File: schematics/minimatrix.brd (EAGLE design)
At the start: 32 x 32 mm, 10 parts

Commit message: ?
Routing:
- net N$2: track 70.4 -> 0.00 mm, vias 1 -> 0
- net GND: track 48.4 -> 0.00 mm, vias 1 -> 0
- net N$9: track 42.3 -> 0.00 mm, vias 3 -> 0
- net N$10: track 41.2 -> 0.00 mm, vias 1 -> 0
- net N$4: track 34.7 -> 0.00 mm
- net VCC: track 32.7 -> 0.00 mm, vias 1 -> 0
- net N$8: track 28.4 -> 0.00 mm
- net N$3: track 26.8 -> 0.00 mm
- net R6: track 25.4 -> 0.00 mm, vias 1 -> 0
- net R3: track 22.8 -> 0.00 mm
- net R8: track 22.2 -> 0.00 mm
- net C6: track 21.5 -> 0.00 mm, vias 1 -> 0
- net ROW1: track 20.3 -> 0.00 mm, vias 1 -> 0
- net R2: track 19.9 -> 0.00 mm, vias 1 -> 0
- net N$6: track 18.4 -> 0.00 mm, vias 1 -> 0
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
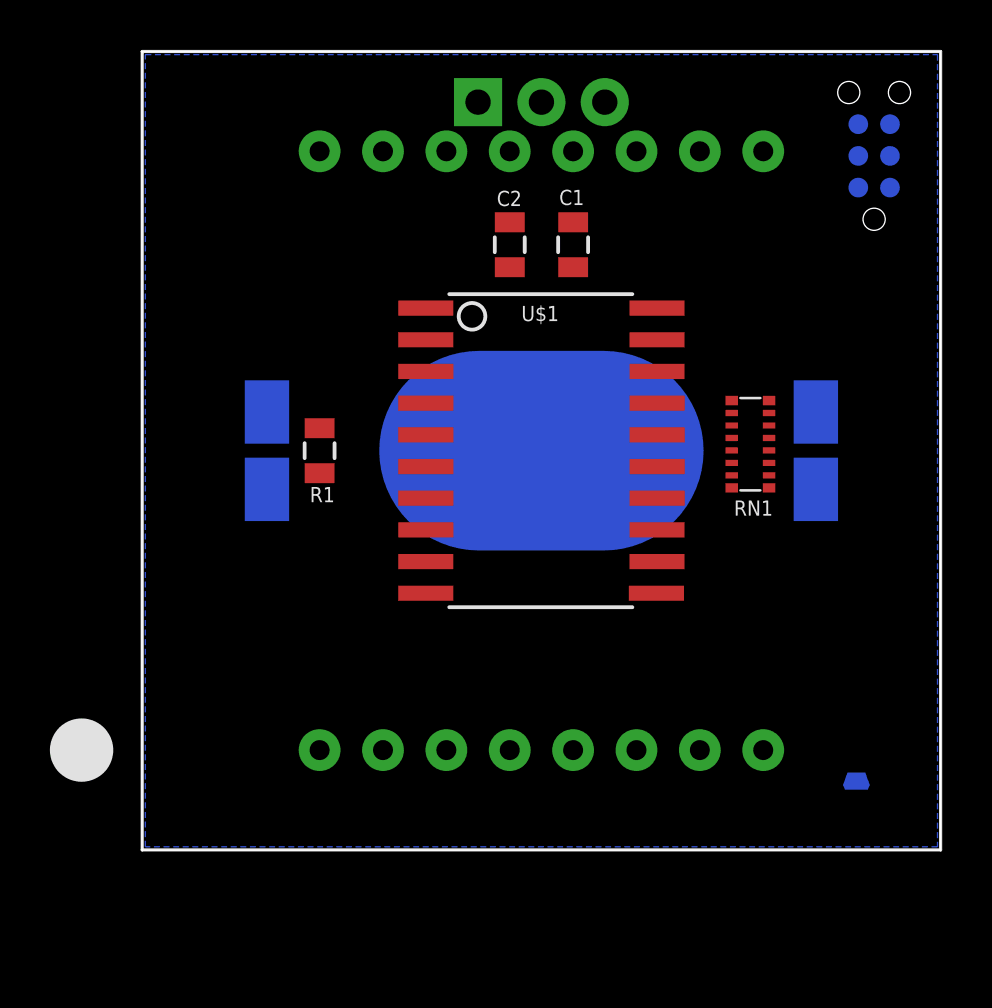
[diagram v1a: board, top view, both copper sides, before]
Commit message: Update design restoring IR receiver.
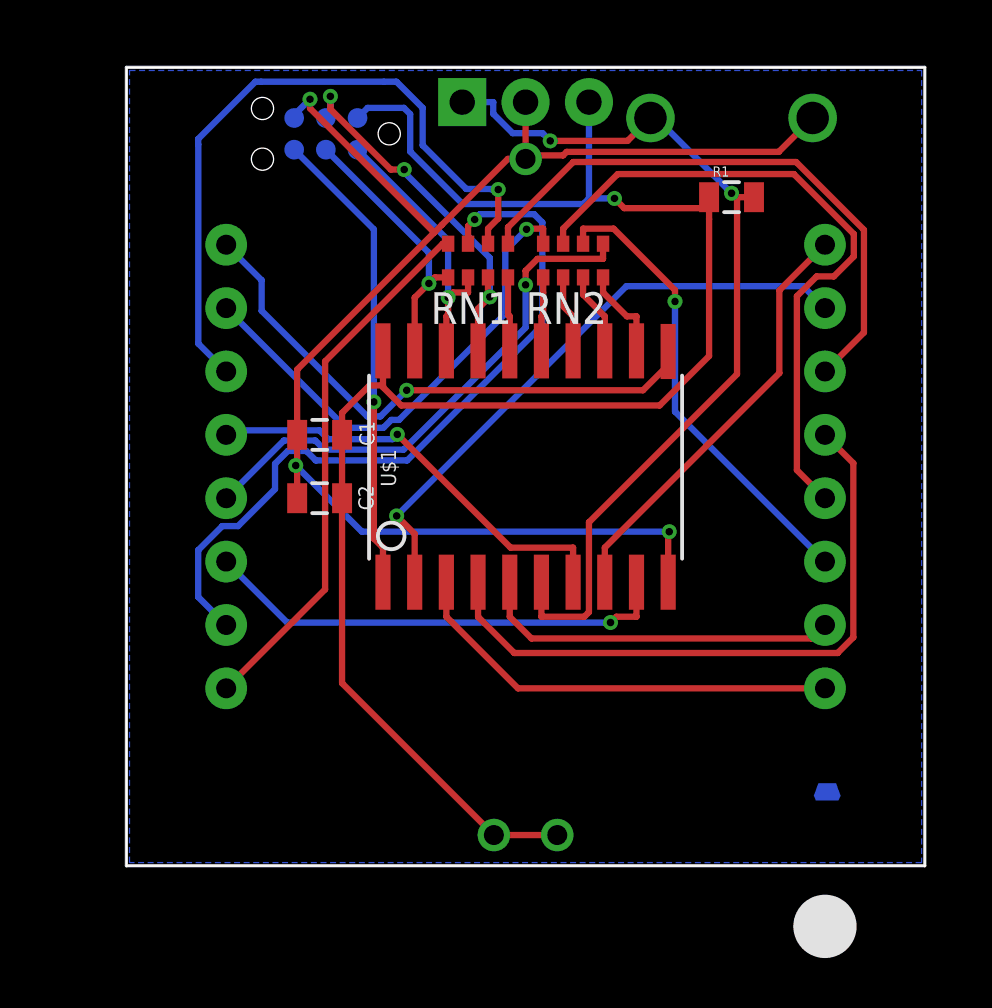
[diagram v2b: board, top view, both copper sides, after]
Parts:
- added RN2: (no value), resistor-dil:CAY16
- added U$5: PNA460XM, adafruit:PNA460XM
- BAT1: value (none) -> BATTERY; device SparkFun-Electromechanical:BATTCON_20MM_4LEGS -> nickparts:COINCELL_PTH
- R1: value 10k -> (none)
- RN1: device resistor-dil:EXB2HV -> resistor-dil:CAY16
- U$2: value PNA460XM -> SWITCH_MOMENTARYRECT; device adafruit:PNA460XM -> nickparts:SWITCH_MOMENTARY_RECT
- moved U$3 19.7 mm to (10.4, 29.2), turned to 0 degrees
- moved R1 19.4 mm to (24.1, 26.7), turned to 0 degrees
- moved RN1 13.2 mm to (14.0, 24.1), turned to 0 degrees
- moved C1 12.7 mm to (7.62, 17.1), turned to 180 degrees
- moved C2 12.7 mm to (7.62, 14.6), turned to 180 degrees
- moved U$2 7.65 mm to (24.1, 29.8)
- moved BAT1 2.01 mm to (15.9, 14.6), turned to 270 degrees
- moved U$4 1.25 mm to (28.0, 3.50)
- moved LED1 0.90 mm to (15.9, 15.9), turned to 90 degrees
- moved U$1 0.90 mm to (15.9, 15.9), turned to 0 degrees
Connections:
- removed net R6: LED1.7, U$1.3
- removed net R8: LED1.5, U$1.5
- removed net ROW5: U$1.4
- new net N$12: LED1.5, U$1.4
- new net N$13: R1.2, U$1.6, U$2.P$1, U$5.1
- net C1: now also RN2.4; no longer RN1.8
- net C2: now also RN2.3; no longer RN1.7
- net C3: now also RN2.2; no longer RN1.6
- net C4: now also RN2.1; no longer RN1.5
- net GND: now also BAT1.NEG, U$2.P$2, U$5.2; no longer BAT1.2, U$2.2
- net N$1: now also LED1.7; no longer R1.1, U$2.1
- net N$10: now also RN2.5; no longer RN1.9
- net N$11: now also U$1.3; no longer R1.2, U$1.6
- net N$3: now also RN2.6; no longer RN1.10
- net N$4: now also RN2.7; no longer RN1.11
- net N$5: now also RN2.8; no longer RN1.12
- net N$6: now also RN1.5; no longer RN1.13
- net N$7: now also RN1.6; no longer RN1.14
- net N$8: now also RN1.7; no longer RN1.15
- net N$9: now also RN1.8; no longer RN1.16
- net R7: now also U$1.5
- net VCC: now also BAT1.POS1, BAT1.POS2, R1.1, U$5.3; no longer BAT1.1, U$2.3
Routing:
- net VCC: track 0.00 -> 66.9 mm, vias 0 -> 1
- net GND: track 0.00 -> 58.8 mm, vias 0 -> 3
- net N$13: track 0.00 -> 36.8 mm, vias 0 -> 2
- net N$8: track 0.00 -> 30.0 mm, vias 0 -> 1
- net N$7: track 0.00 -> 28.0 mm, vias 0 -> 1
- net N$4: track 0.00 -> 26.6 mm
- net N$12: track 0.00 -> 25.9 mm
- net N$1: track 0.00 -> 24.3 mm, vias 0 -> 1
- net N$6: track 0.00 -> 23.5 mm
- net ROW1: track 0.00 -> 22.7 mm, vias 0 -> 1
- net N$9: track 0.00 -> 21.6 mm
- net N$10: track 0.00 -> 21.3 mm, vias 0 -> 1
- net N$5: track 0.00 -> 20.1 mm, vias 0 -> 1
- net R2: track 0.00 -> 18.9 mm, vias 0 -> 1
- net N$2: track 0.00 -> 18.8 mm, vias 0 -> 1
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
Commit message: Tweaks for production version
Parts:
- renumbered U$1 to IC1, U$2 to SW1, U$5 to IC2
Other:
- board text added: "IR receiver BEFORE"
- board text added: "Minimatrix 1.0"
- board text added: "Solder the battery"
- board text added: "WARNING!"
- board text added: "holder, switch, and"
- board text added: "matrix!"
- board text added: "soldering the LED"
- board text removed: "Minimatrix by Arachnid Labs"

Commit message: Numerous changes and improvements
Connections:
- net C1 renamed COL1
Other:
- board text added: "www.arachnidlabs.com"
- board text removed: "www.arachnidlabs.com/minimatrix/"
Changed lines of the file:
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@@
 <?xml version="1.0" encoding="utf-8"?>
 <!DOCTYPE eagle SYSTEM "eagle.dtd">
-<eagle version="6.2">
+<eagle version="6.4">
 <drawing>
 <settings>
@@
 <wire x1="-0.115" y1="31.865" x2="-0.115" y2="-0.135" width="0" layer="20"/>
 <wire x1="-0.115" y1="-0.135" x2="31.885" y2="-0.135" width="0" layer="20"/>
-<text x="6.35" y="1.905" size="1.016" layer="26" font="vector" rot="MR0" align="bottom-center">Minimatrix 1.0</text>
-<text x="6.35" y="1.27" size="0.4064" layer="26" font="vector" ratio="9" rot="MR0" align="bottom-center">www.arachnidlabs.com/minimatrix/</text>
+<text x="6.35" y="1.905" size="1.016" layer="26" font="vector" ratio="10" rot="MR0" align="bottom-center">Minimatrix 1.0</text>
+<text x="6.35" y="0.635" size="0.762" layer="26" font="vector" ratio="10" rot="MR0" align="bottom-center">www.arachnidlabs.com</text>
 <text x="15.875" y="24.13" size="1.016" layer="26" font="vector" ratio="9" rot="MR0" align="bottom-center">WARNING!</text>
 <text x="15.875" y="21.59" size="0.8128" layer="26" font="vector" ratio="9" rot="MR0" align="bottom-center">Solder the battery</text>
@@
 </class>
 </classes>
-<designrules>
+<designrules name="default">
 <description language="de">&lt;b&gt;EAGLE Design Rules&lt;/b&gt;
 &lt;p&gt;
@@
 <wire x1="27.3342" y1="8.9842" x2="27.875" y2="9.525" width="0.254" layer="1"/>
 </signal>
-<signal name="C1">
+<signal name="COL1">
 <contactref element="IC1" pad="12"/>
 <contactref element="RN2" pad="4"/>
@@
 </signal>
 </signals>
-<errors>
-</errors>
 </board>
 </drawing>

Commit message: Work on programmer code; don't accept commands when asleep
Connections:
- net C6 renamed MOSI
- net C7 renamed MISO
- net C8 renamed SCK
- net N$2 renamed RESET
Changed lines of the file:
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@@
 <wire x1="9.545" y1="30.25" x2="9.14" y2="29.845" width="0.254" layer="16"/>
 </signal>
-<signal name="C8">
+<signal name="SCK">
 <contactref element="IC1" pad="19"/>
 <contactref element="U$3" pad="3"/>
@@
 <via x="12.0005" y="23.2151" extent="1-16" drill="0.3" diameter="0.6048"/>
 </signal>
-<signal name="N$2">
+<signal name="RESET">
 <contactref element="IC1" pad="1"/>
 <contactref element="U$3" pad="5"/>
@@
 <via x="9.7947" y="18.4643" extent="1-16" drill="0.3" diameter="0.6048"/>
 </signal>
-<signal name="C6">
+<signal name="MOSI">
 <contactref element="U$3" pad="4"/>
 <contactref element="IC1" pad="17"/>
@@
 <wire x1="13.97" y1="20.5105" x2="13.97" y2="21.8949" width="0.254" layer="1"/>
 </signal>
-<signal name="C7">
+<signal name="MISO">
 <contactref element="U$3" pad="1"/>
 <contactref element="IC1" pad="18"/>
